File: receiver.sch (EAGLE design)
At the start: 33 parts

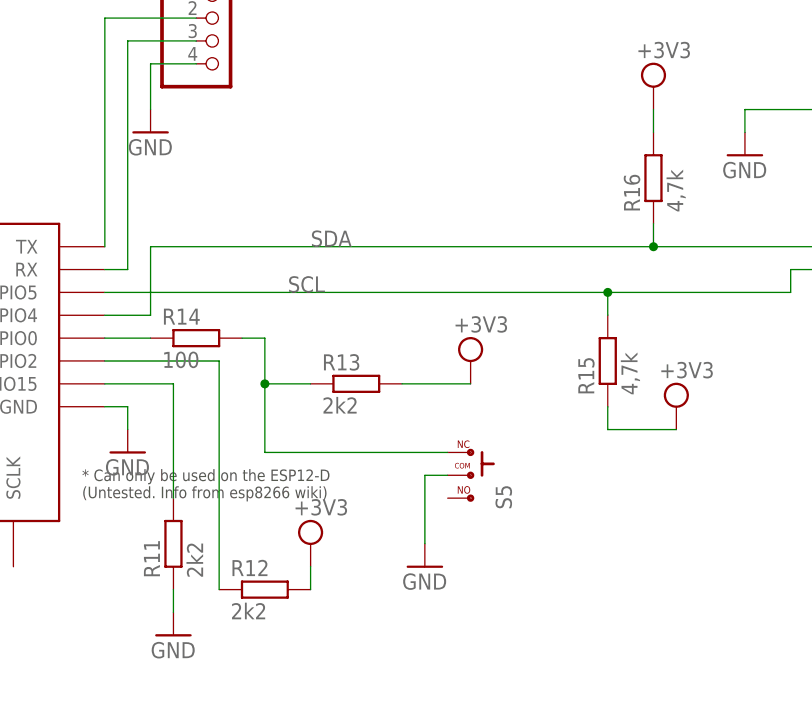
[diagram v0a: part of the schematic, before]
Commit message: Corrected programming switch connection.
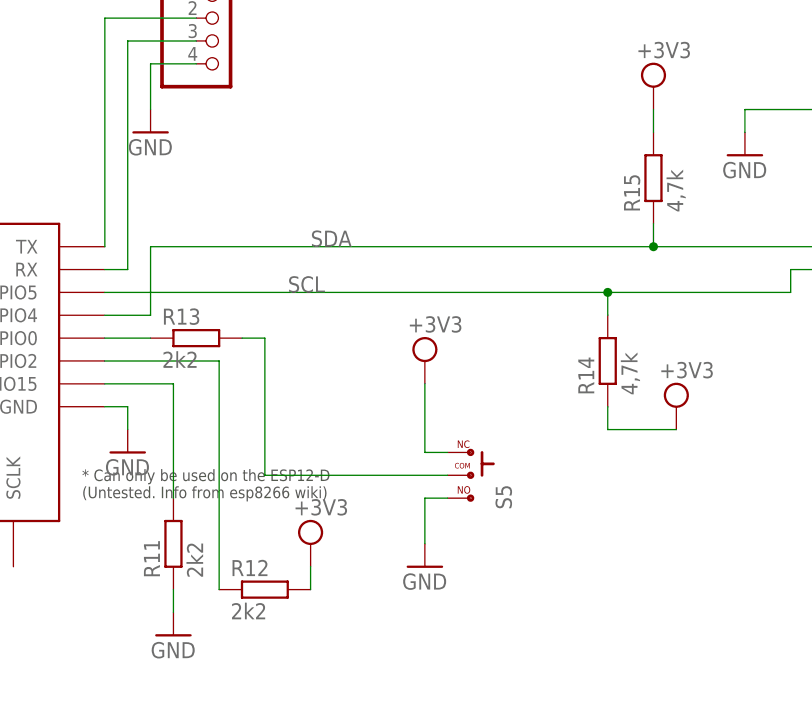
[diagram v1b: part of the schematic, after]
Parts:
- removed R16: 4,7k, rcl:R-EU_0204/7
- R14: value 100 -> 4,7k
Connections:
- net GND: now also S5.3; no longer S5.2
- net N$19: now also R13.1; no longer R14.1
- net N$3: now also R13.2, S5.2; no longer R13.1, R14.2, S5.1
- net SCL: now also R14.2; no longer R15.2
- net SDA: now also R15.1; no longer R16.1
- net VCC: now also R14.1, R15.2, S5.1; no longer R13.2, R15.1, R16.2
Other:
- moved on the sheet: R13, R14, R15
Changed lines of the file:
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@@
 <part name="R1" library="rcl" library_urn="urn:adsk.eagle:library:334" deviceset="R-EU_" device="0204/7" package3d_urn="urn:adsk.eagle:package:23498/1" value="10k"/>
 <part name="GND9" library="supply1" library_urn="urn:adsk.eagle:library:371" deviceset="GND" device=""/>
+<part name="R14" library="rcl" library_urn="urn:adsk.eagle:library:334" deviceset="R-EU_" device="0204/7" package3d_urn="urn:adsk.eagle:package:23498/1" value="4,7k"/>
 <part name="R15" library="rcl" library_urn="urn:adsk.eagle:library:334" deviceset="R-EU_" device="0204/7" package3d_urn="urn:adsk.eagle:package:23498/1" value="4,7k"/>
-<part name="R16" library="rcl" library_urn="urn:adsk.eagle:library:334" deviceset="R-EU_" device="0204/7" package3d_urn="urn:adsk.eagle:package:23498/1" value="4,7k"/>
 <part name="SUPPLY17" library="supply2" library_urn="urn:adsk.eagle:library:372" deviceset="VCC" device="" value="+3V3"/>
 <part name="SUPPLY18" library="supply2" library_urn="urn:adsk.eagle:library:372" deviceset="VCC" device="" value="+3V3"/>
@@
 <part name="GND13" library="supply1" library_urn="urn:adsk.eagle:library:371" deviceset="GND" device=""/>
 <part name="R4" library="rcl" library_urn="urn:adsk.eagle:library:334" deviceset="R-EU_" device="0204/7" package3d_urn="urn:adsk.eagle:package:23498/1" value="1k"/>
-<part name="R14" library="rcl" library_urn="urn:adsk.eagle:library:334" deviceset="R-EU_" device="0204/7" package3d_urn="urn:adsk.eagle:package:23498/1" value="100"/>
 <part name="R2" library="rcl" library_urn="urn:adsk.eagle:library:334" deviceset="R-EU_" device="0204/7" package3d_urn="urn:adsk.eagle:package:23498/1" value="100"/>
 <part name="S2" library="switch-tact" deviceset="DTS-6" device=""/>
@@
 <instance part="C2" gate="G$1" x="12.7" y="114.3"/>
 <instance part="GND8" gate="1" x="10.16" y="101.6"/>
-<instance part="R13" gate="G$1" x="101.6" y="58.42"/>
+<instance part="R13" gate="G$1" x="83.82" y="63.5"/>
 <instance part="GND10" gate="1" x="27.94" y="27.94"/>
 <instance part="R8" gate="G$1" x="25.4" y="60.96"/>
@@
 <instance part="GND12" gate="1" x="81.28" y="30.48"/>
 <instance part="SUPPLY1" gate="G$1" x="76.2" y="106.68"/>
-<instance part="SUPPLY2" gate="G$1" x="114.3" y="60.96"/>
+<instance part="SUPPLY2" gate="G$1" x="109.22" y="60.96"/>
 <instance part="SUPPLY5" gate="G$1" x="96.52" y="40.64"/>
 <instance part="SUPPLY8" gate="G$1" x="25.4" y="101.6"/>
@@
 <instance part="R1" gate="G$1" x="25.4" y="91.44" rot="R90"/>
 <instance part="GND9" gate="1" x="0" y="73.66"/>
-<instance part="R15" gate="G$1" x="129.54" y="60.96" rot="R90"/>
-<instance part="R16" gate="G$1" x="134.62" y="81.28" rot="R90"/>
+<instance part="R14" gate="G$1" x="129.54" y="60.96" rot="R90"/>
+<instance part="R15" gate="G$1" x="134.62" y="81.28" rot="R90"/>
 <instance part="SUPPLY17" gate="G$1" x="134.62" y="91.44"/>
 <instance part="SUPPLY18" gate="G$1" x="137.16" y="55.88"/>
@@
 <instance part="GND13" gate="1" x="-20.32" y="63.5"/>
 <instance part="R4" gate="G$1" x="0" y="66.04"/>
-<instance part="R14" gate="G$1" x="83.82" y="63.5"/>
 <instance part="R2" gate="G$1" x="33.02" y="78.74"/>
 <instance part="S2" gate="G$1" x="-12.7" y="45.72"/>
@@
 </segment>
 <segment>
-<pinref part="R13" gate="G$1" pin="2"/>
-<wire x1="106.68" y1="58.42" x2="114.3" y2="58.42" width="0.1524" layer="91"/>
-<pinref part="SUPPLY2" gate="G$1" pin="VCC"/>
-</segment>
-<segment>
 <pinref part="R12" gate="G$1" pin="2"/>
 <wire x1="96.52" y1="35.56" x2="96.52" y2="38.1" width="0.1524" layer="91"/>
@@
 </segment>
 <segment>
-<pinref part="R16" gate="G$1" pin="2"/>
+<pinref part="R15" gate="G$1" pin="2"/>
 <pinref part="SUPPLY17" gate="G$1" pin="VCC"/>
 <wire x1="134.62" y1="86.36" x2="134.62" y2="88.9" width="0.1524" layer="91"/>
 </segment>
 <segment>
-<pinref part="R15" gate="G$1" pin="1"/>
+<pinref part="R14" gate="G$1" pin="1"/>
 <wire x1="129.54" y1="55.88" x2="129.54" y2="53.34" width="0.1524" layer="91"/>
 <wire x1="129.54" y1="53.34" x2="137.16" y2="53.34" width="0.1524" layer="91"/>
@@
 <wire x1="35.56" y1="132.08" x2="40.64" y2="132.08" width="0.1524" layer="91"/>
 </segment>
+<segment>
+<pinref part="S5" gate="G$1" pin="1"/>
+<wire x1="111.76" y1="50.8" x2="109.22" y2="50.8" width="0.1524" layer="91"/>
+<wire x1="109.22" y1="50.8" x2="109.22" y2="58.42" width="0.1524" layer="91"/>
+<pinref part="SUPPLY2" gate="G$1" pin="VCC"/>
+</segment>
 </net>
 <net name="GND" class="0">
@@
 <wire x1="5.08" y1="81.28" x2="5.08" y2="78.74" width="0.1524" layer="91"/>
 <junction x="5.08" y="78.74"/>
-</segment>
-<segment>
-<pinref part="S5" gate="G$1" pin="2"/>
-<wire x1="109.22" y1="40.64" x2="109.22" y2="48.26" width="0.1524" layer="91"/>
-<wire x1="109.22" y1="48.26" x2="111.76" y2="48.26" width="0.1524" layer="91"/>
-<pinref part="GND14" gate="1" pin="GND"/>
 </segment>
 <segment>
@@
 <junction x="30.48" y="134.62"/>
 </segment>
+<segment>
+<pinref part="S5" gate="G$1" pin="3"/>
+<wire x1="111.76" y1="45.72" x2="109.22" y2="45.72" width="0.1524" layer="91"/>
+<pinref part="GND14" gate="1" pin="GND"/>
+<wire x1="109.22" y1="45.72" x2="109.22" y2="40.64" width="0.1524" layer="91"/>
+</segment>
 </net>
 <net name="N$2" class="0">
@@
 <segment>
 <label x="93.98" y="68.58" size="1.778" layer="95"/>
-<pinref part="R15" gate="G$1" pin="2"/>
+<pinref part="R14" gate="G$1" pin="2"/>
 <wire x1="129.54" y1="66.04" x2="129.54" y2="68.58" width="0.1524" layer="91"/>
 <junction x="129.54" y="68.58"/>
@@
 <wire x1="78.74" y1="66.04" x2="78.74" y2="73.66" width="0.1524" layer="91"/>
 <label x="96.52" y="73.66" size="1.778" layer="95"/>
-<pinref part="R16" gate="G$1" pin="1"/>
+<pinref part="R15" gate="G$1" pin="1"/>
 <wire x1="134.62" y1="76.2" x2="134.62" y2="73.66" width="0.1524" layer="91"/>
 <wire x1="78.74" y1="73.66" x2="134.62" y2="73.66" width="0.1524" layer="91"/>
@@
 <net name="N$3" class="0">
 <segment>
-<wire x1="91.44" y1="63.5" x2="91.44" y2="58.42" width="0.1524" layer="91"/>
-<wire x1="91.44" y1="58.42" x2="96.52" y2="58.42" width="0.1524" layer="91"/>
-<pinref part="R13" gate="G$1" pin="1"/>
-<pinref part="R14" gate="G$1" pin="2"/>
 <wire x1="88.9" y1="63.5" x2="91.44" y2="63.5" width="0.1524" layer="91"/>
-<pinref part="S5" gate="G$1" pin="1"/>
-<wire x1="111.76" y1="50.8" x2="91.44" y2="50.8" width="0.1524" layer="91"/>
-<wire x1="91.44" y1="58.42" x2="91.44" y2="50.8" width="0.1524" layer="91"/>
-<junction x="91.44" y="58.42"/>
+<wire x1="91.44" y1="63.5" x2="91.44" y2="48.26" width="0.1524" layer="91"/>
+<pinref part="R13" gate="G$1" pin="2"/>
+<pinref part="S5" gate="G$1" pin="2"/>
+<wire x1="91.44" y1="48.26" x2="111.76" y2="48.26" width="0.1524" layer="91"/>
 </segment>
 </net>
@@
 <net name="N$19" class="0">
 <segment>
-<pinref part="R14" gate="G$1" pin="1"/>
 <pinref part="ESP-12E" gate="G$1" pin="GPIO0"/>
 <wire x1="78.74" y1="63.5" x2="73.66" y2="63.5" width="0.1524" layer="91"/>
-</segment>
-</net>
+<pinref part="R13" gate="G$1" pin="1"/>
+</segment>
+</net>
